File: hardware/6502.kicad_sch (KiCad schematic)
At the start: 61 parts, among them J1 JMP, J10 JMP, J12 Control_bus, J13 EzRST, J14 Power, J15 Data_bus, J16 Address bus, J17 JMP, J18 JMP, J19 JMP, J2 PORTAB, J20 Interface, J3 CA, J4 CB, J5 W27c512?, J8 Barrel_Jack_MountingPin, J9 USB_B_Micro, SW1 SW_Push, U1 74HC14, U14 74HC04, U15 MIC5504-3.3YM5, U17 74HC00, U2 R6502, U3 R6522, U4 74HC273, U5 SST39SF010, U9 NRF24L01_Breakout

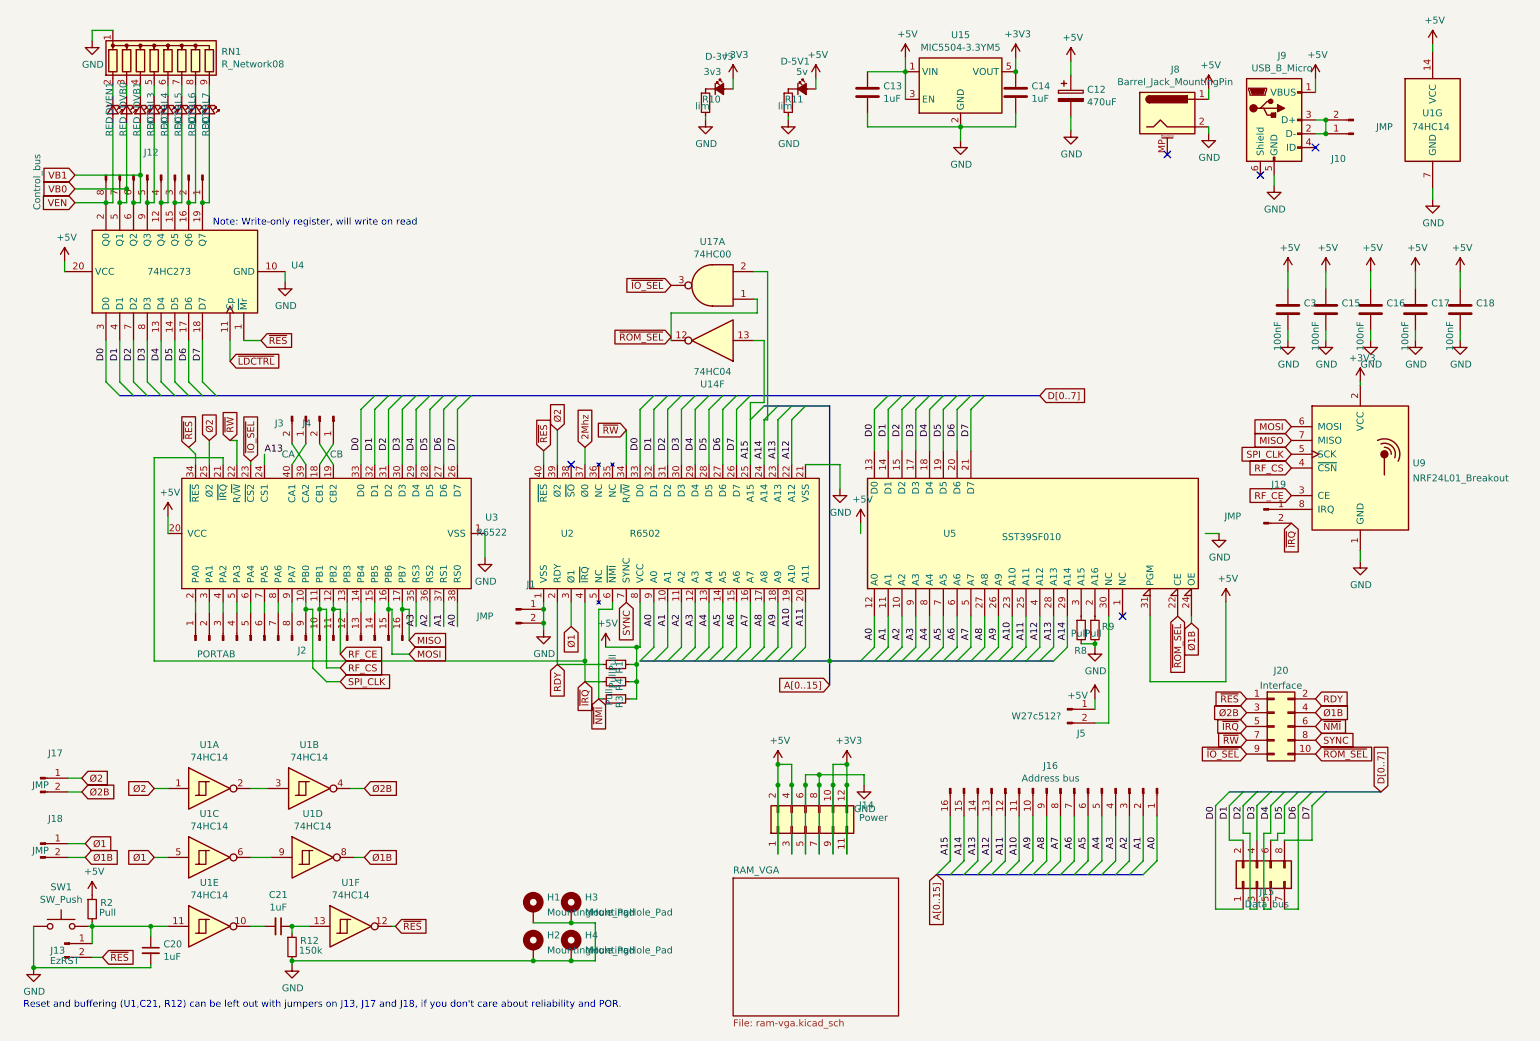
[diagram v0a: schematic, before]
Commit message: PS/2 via shift register upgrade!
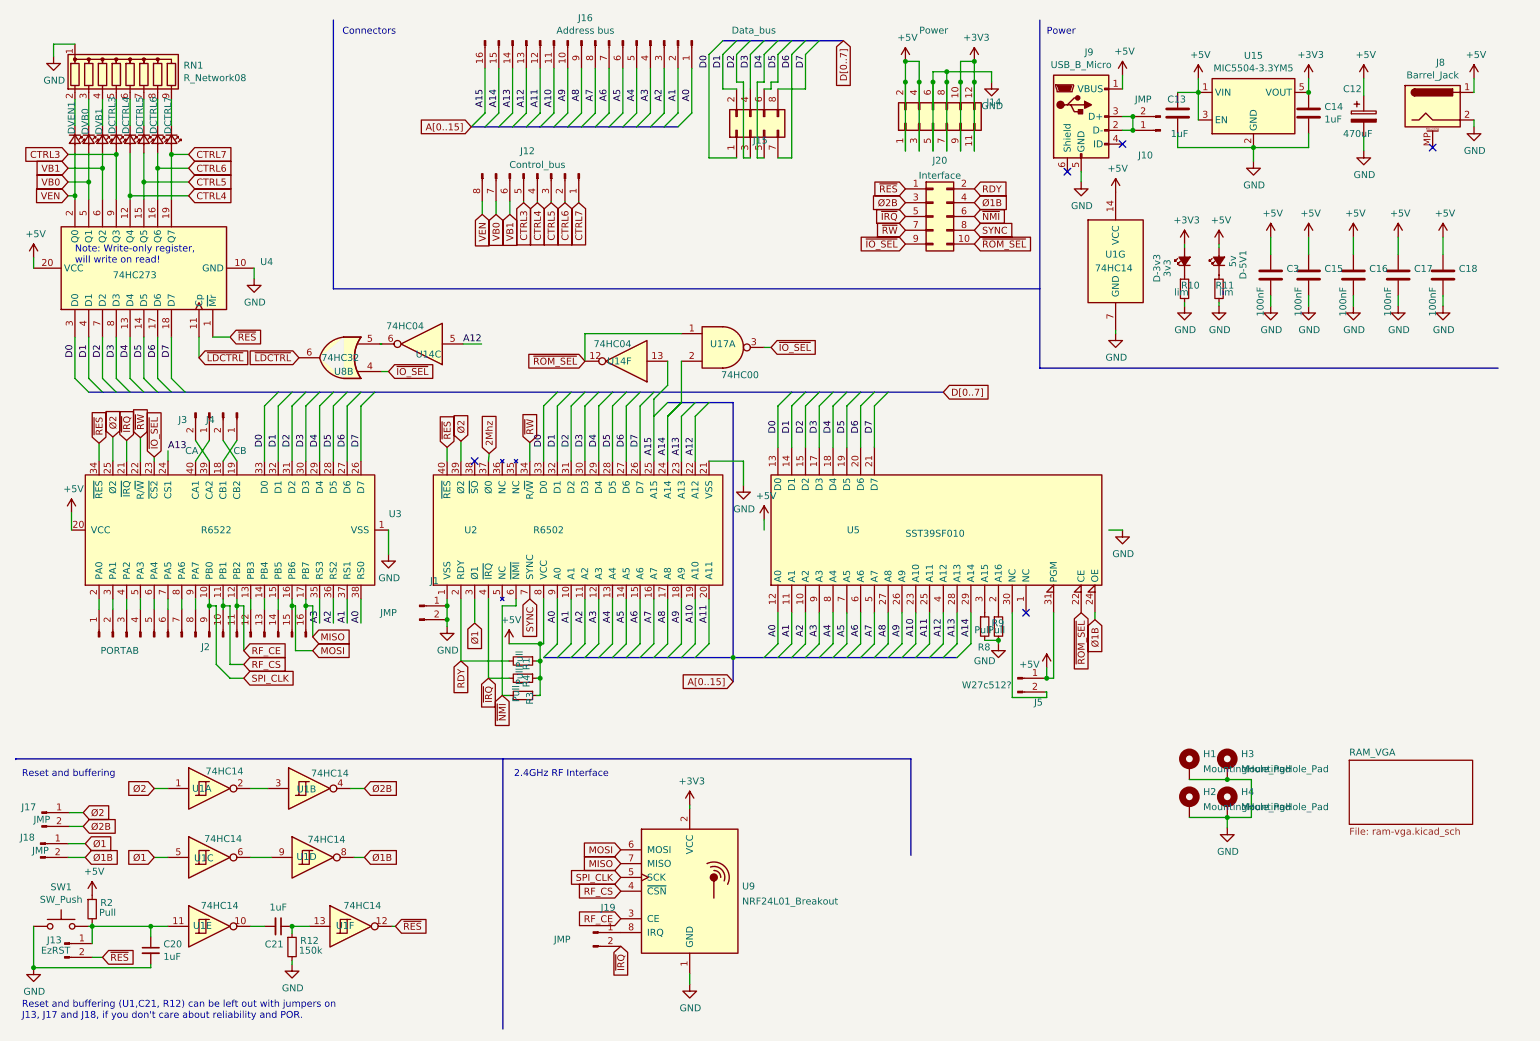
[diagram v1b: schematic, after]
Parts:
- added unit 3 of U14
- added U8: 74HC32, Package_DIP:DIP-14_W7.62mm, symbol 74xx:74LS32
- J8: value Barrel_Jack_MountingPin -> Barrel_Jack
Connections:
- net A12: now also U14.5
- net ~{IO_SEL}: now also U8.4
- net ~{LDCTRL}: now also U8.6
- net CTRL4: now reaches DCTRL4.2 (A), J12.4 (Pin_4), U4.12 (Q4)
- net CTRL5: now reaches DCTRL5.2 (A), J12.3 (Pin_3), U4.15 (Q5)
- net CTRL6: now reaches DCTRL6.2 (A), J12.2 (Pin_2), U4.16 (Q6)
- net CTRL7: now reaches DCTRL7.2 (A), J12.1 (Pin_1), U4.19 (Q7)
- net CTRL3: now reaches DCTRL3.2 (A), J12.5 (Pin_5), U4.9 (Q3)
- new net: U14.6, U8.5
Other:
- note added: "2.4GHz RF Interface"
- note added: "Connectors"
- note added: "Note: Write-only register, will write on read!"
- note added: "Power"
- note added: "Reset and buffering"
- note removed: "Note: Write-only register, will write on read"
- moved on the sheet: C12, C13, C14, C15, C16, C17, C18, C3, D-3v3, D-5V1, DCTRL3, DCTRL4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

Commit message: R1B2 gerbers, start+stop bits in modem driver
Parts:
- removed J13: EzRST, Connector_PinHeader_2.54mm:PinHeader_1x02_P2.54mm_Vertical, symbol Connector:Conn_01x02_Male
- removed J17, J18, J19: JMP, Connector_PinHeader_2.54mm:PinHeader_1x02_P2.54mm_Vertical, symbol Connector:Conn_01x02_Male
- removed J8: Barrel_Jack, Connector_BarrelJack:BarrelJack_Horizontal, symbol Connector:Barrel_Jack_MountingPin
- removed unit 3 of U14
- added C22: 10uF, Capacitor_SMD:C_0805_2012Metric, symbol Device:C_Small
- added C23, C24, C25: 100nF, Capacitor_SMD:C_0603_1608Metric, symbol Device:C_Small
- added J17: USB_A, Connector_USB:USB_A_Molex_67643_Horizontal, symbol Connector:USB_A
- added J8: 5V, Connector_PinHeader_2.54mm:PinHeader_1x02_P2.54mm_Vertical, symbol Connector:Conn_01x02_Male
- added R28: 0R, Resistor_SMD:R_0402_1005Metric_Pad0.72x0.64mm_HandSolder, symbol Device:R_Small
- added R29, R47: NC, Resistor_SMD:R_0402_1005Metric_Pad0.72x0.64mm_HandSolder, symbol Device:R_Small
- added R48: 0R, Resistor_SMD:R_0805_2012Metric, symbol Device:R_Small
- added R49: NC, Resistor_SMD:R_0805_2012Metric, symbol Device:R_Small
- added U13: 74HC74, Package_DIP:DIP-14_W7.62mm, symbol 74xx:74HC74
- added unit 4 of U14
- added U21: 74HC00, Package_DIP:DIP-14_W7.62mm, symbol 74xx:74HC00
- C13, C14, C15, C16, C17, C18, C3: symbol Device:C -> Device:C_Small
- J1: value JMP -> 5V
- renumbered D-3v3 to 3v3, D-5V1 to 5V0
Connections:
- net +5V: now also J1.1 (Pin_1), C22.1, C23.1, C24.1, C25.1, J17.1 (VBUS), J8.1 (Pin_1), U13.1 (~{R}), U13.10 (~{S}), U13.13 (~{R}), U13.14 (VCC), U13.4 (~{S}), U21.14 (VCC)
- net 2Mhz: now also J20.3 (Pin_3), R47.1, U13.3 (C)
- net A12: now also U1.3, U21.1
- net A13: now also U21.12, U21.2; no longer U3.24 (CS1)
- net GND: now also C22.2, C23.2, C24.2, C25.2, J17.4 (GND), J17.5 (Shield), J8.2 (Pin_2), R28.2, U13.11 (C), U13.12 (D), U13.7 (GND), U14.9, U21.7 (GND); no longer J1.1 (Pin_1), U2.1 (VSS)
- net MISO: now also J2.14 (Pin_14), U3.15 (PB5); no longer J2.16 (Pin_16), U3.17 (PB7)
- net MOSI: now also J2.16 (Pin_16), U3.17 (PB7); no longer J2.15 (Pin_15), U3.16 (PB6)
- net SPI_CLK: now also R49.1
- net ~{IRQ}: now also R29.2
- net ~{RW}: now also U1.1
- net Ø1: no longer U1.5
- net Ø1B: no longer U1.8
- net Ø2: no longer U1.1
- net at U2.36 (NC/BE): now also R47.2
- net SDA_VGA: now reaches J2.12 (Pin_12), U3.13 (PB3)
- net at J2.13 (Pin_13), U3.14 (PB4): now also R48.1
- net CB1: now reaches J4.1 (Pin_1), U3.18 (CB1)
- net CB1: now also U13.6 (~{Q})
- net CB2: now reaches J4.2 (Pin_2), U3.19 (CB2)
- net CB2: now also J17.2 (D-)
- net at U1.2: now also U21.5; no longer U1.3
- net at U1.9: now also U21.3; no longer U1.6
- net at U9.8 (IRQ): now also R29.1
- net at U8.5: now also U21.6
- net ~{LDCTRL}: no longer names the net of U4.11 (Cp), U8.6
- net Ø2B: no longer names the net of U1.4
- net Ø2B: now also U21.13; no longer J20.3 (Pin_3)
- new net: R28.1, U2.1 (VSS)
- new net: U1.8, U21.4
- new net: U1.5, U21.11
- new net PB6: J17.3 (D+), J2.15 (Pin_15), U13.2 (D), U3.16 (PB6)
- new net SCL_VGA: R48.2, R49.2
- new net VIACS1: U1.6, U3.24 (CS1)
- no-connect marks 5 -> 8
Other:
- note added: "Note: Write-only register - cannot be read."
- note added: "PS2 keyboard interface"
- note added: "R65C02, 6502 = 0R WDC65C02 = NC."
- note added: "Reset circuit"
- note added: "Select resistors for i2c SCL"
- note removed: "Note: Write-only register, will write on read!"
- note removed: "Reset and buffering"
- note removed: "Reset and buffering (U1,C21, R12) can be left out with jumpers on J13, J17 and J18, if you don't care about reliability and POR."
- moved on the sheet: 3v3, 5V0, C12, C13, C14, C15, C16, C17, C18, C3, J10, J9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

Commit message: Solder jumpers instead of 0402 resistors, redundant 0805 decoupling caps
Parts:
- added C26, C27, C28, C29, C30, C31, C32, C33, C34, C35, C36, C37: NC, Capacitor_SMD:C_0805_2012Metric, symbol Device:C_Small
- R28, R29, R47: footprint Resistor_SMD:R_0402_1005Metric_Pad0.72x0.64mm_HandSolder -> Jumper:SolderJumper-2_P1.3mm_Open_RoundedPad1.0x1.5mm
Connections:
- net +5V: now also C26.1, C27.1, C28.1, C29.1, C30.1, C31.1, C32.1, C33.1, C34.1, C35.1, C36.1, C37.1
- net GND: now also C26.2, C27.2, C28.2, C29.2, C30.2, C31.2, C32.2, C33.2, C34.2, C35.2, C36.2, C37.2
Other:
- note added: "Note: Write-only register @ $7000 - cannot be read."
- note removed: "Note: Write-only register - cannot be read."
- title: ABNielsen.com 6502 Single Board Computer -> ABNielsen.com 6502 Single Board Computer R1 B3

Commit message: Silkscreen indicators, updated BOM and gerbers and stuff
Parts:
- 3v3, 5V0, DCTRL3, DCTRL4, DCTRL5, DCTRL6, DCTRL7, DVB0, DVB1, DVEN1: LCSC (none) -> C84256
- C12: value 470uF -> 220uF; LCSC (none) -> C131120
- J9: footprint Connector_USB:USB-B-MICRO-SMD_V03-fixed -> Connector_USB:USB_Micro-B_Amphenol_10118194_Horizontal; LCSC (none) -> C132563
- R1, R2, R3, R4, R8, R9: value Pull -> 3k
- R10, R11: value lim -> 3k
- SW1: LCSC (none) -> C318884
- U15: LCSC (none) -> C3021093
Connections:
- net GND: now also J9.6 (Shield)
- no-connect marks 8 -> 7
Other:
- title: ABNielsen.com 6502 Single Board Computer R1 B3 -> ABNielsen.com 6502 Single Board Computer R1 B4

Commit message: Revision 2 published
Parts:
- removed J9: USB_B_Micro, Connector_USB:USB_Micro-B_Amphenol_10118194_Horizontal, symbol 6502-rescue:USB_B_Micro-Connector
- removed R48: 0R, Resistor_SMD:R_0805_2012Metric, symbol Device:R_Small
- removed RN1: R_Network08, Resistor_THT:R_Array_SIP9, symbol Device:R_Network08
- added J9: USB2.0_16P, Connector_USB:USB_C_Receptacle_HCTL_HC-TYPE-C-16P-01A, symbol Connector:USB_C_Receptacle_USB2.0_16P
- added R48: 0R, Jumper:SolderJumper-2_P1.3mm_Bridged_RoundedPad1.0x1.5mm, symbol Jumper:SolderJumper_2_Bridged
- added R50, R51, R52, R53, R54, R55, R56, R57: 3k, Resistor_SMD:R_0805_2012Metric, symbol Device:R_Small
- added R58, R59: 5k1, Resistor_SMD:R_0805_2012Metric, symbol Device:R_Small
- C13, C14, C20, C21: LCSC (none) -> C28323
- C15, C16, C17, C18, C23, C24, C25, C3: LCSC (none) -> C14663
- J10: value JMP -> USB
- J14: LCSC (none) -> C92269
- J15: LCSC (none) -> C92271
- J16: LCSC (none) -> C30734
- J17: LCSC (none) -> C456018
- J2: LCSC (none) -> C7500783
- J20: LCSC (none) -> C2685204
- J3, J4: LCSC (none) -> C7499322
- R1, R10, R11, R2, R3, R4, R8, R9: LCSC (none) -> C17661
- R12: LCSC (none) -> C17470
- R28: footprint Jumper:SolderJumper-2_P1.3mm_Open_RoundedPad1.0x1.5mm -> Jumper:SolderJumper-2_P1.3mm_Bridged_RoundedPad1.0x1.5mm; symbol Device:R_Small -> Jumper:SolderJumper_2_Bridged; now left out of the parts list
- U1, U13, U14, U17, U21, U8: LCSC (none) -> C2325
- U2, U3: LCSC (none) -> C72123
- U4: LCSC (none) -> C72118
- U5: LCSC (none) -> C146583
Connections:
- net +5V: now also J9.A4 (VBUS), J9.A9 (VBUS), J9.B4 (VBUS), J9.B9 (VBUS)
- net GND: now also R28.1 (A), J9.A1 (GND), J9.A12 (GND), J9.B1 (GND), J9.B12 (GND), J9.S1 (SHIELD), R50.1, R51.1, R52.1, R53.1, R54.1, R55.1, R56.1, R57.1, R58.2, R59.2; no longer R28.2
- net SCL_VGA: now also R48.1 (A)
- net at U2.1 (VSS): now also R28.2 (B); no longer R28.1
- net at DVEN1.1 (K): now also R57.2
- net at DVB0.1 (K): now also R56.2
- net at DVB1.1 (K): now also R55.2
- net at DCTRL3.1 (K): now also R54.2
- net at DCTRL4.1 (K): now also R53.2
- net at DCTRL5.1 (K): now also R52.2
- net at DCTRL6.1 (K): now also R51.2
- net at DCTRL7.1 (K): now also R50.2
- net at J2.13 (Pin_13), U3.14 (PB4): now also R48.2 (B)
- net at J10.1 (Pin_1): now also J9.A6 (D+), J9.B6 (D+); no longer J10.2 (Pin_2)
- new net: J9.B5 (CC2), R59.1
- new net: J9.A5 (CC1), R58.1
- new net: J10.2 (Pin_2), J9.A7 (D-), J9.B7 (D-)
- no-connect marks 7 -> 8
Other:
- note added: "R65C02, 6502 = Closed WDC65C02 = Cut"
- note removed: "R65C02, 6502 = 0R WDC65C02 = NC."
- title: ABNielsen.com 6502 Single Board Computer R1 B4 -> ABNielsen.com 6502 Single Board Computer Rev. 2
- moved on the sheet: 3v3, 5V0, C12, C13, C14, C15, C16, C17, C18, C22, C23, C24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
